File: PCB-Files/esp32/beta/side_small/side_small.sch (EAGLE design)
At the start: 9 parts

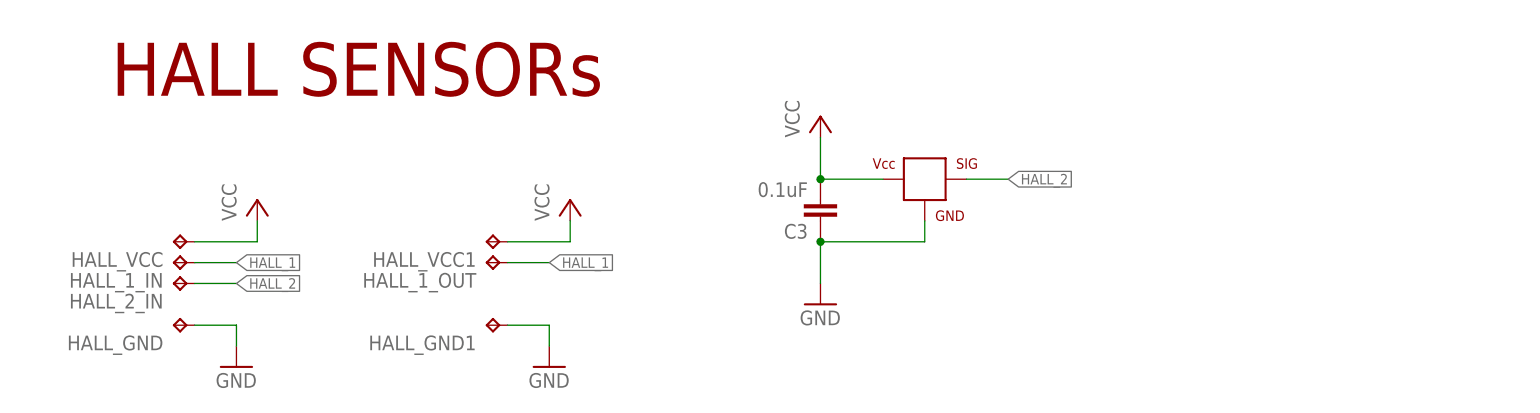
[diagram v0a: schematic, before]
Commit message: creates final PCB version; revised beta side pcbs to match beta main pcb pinouts
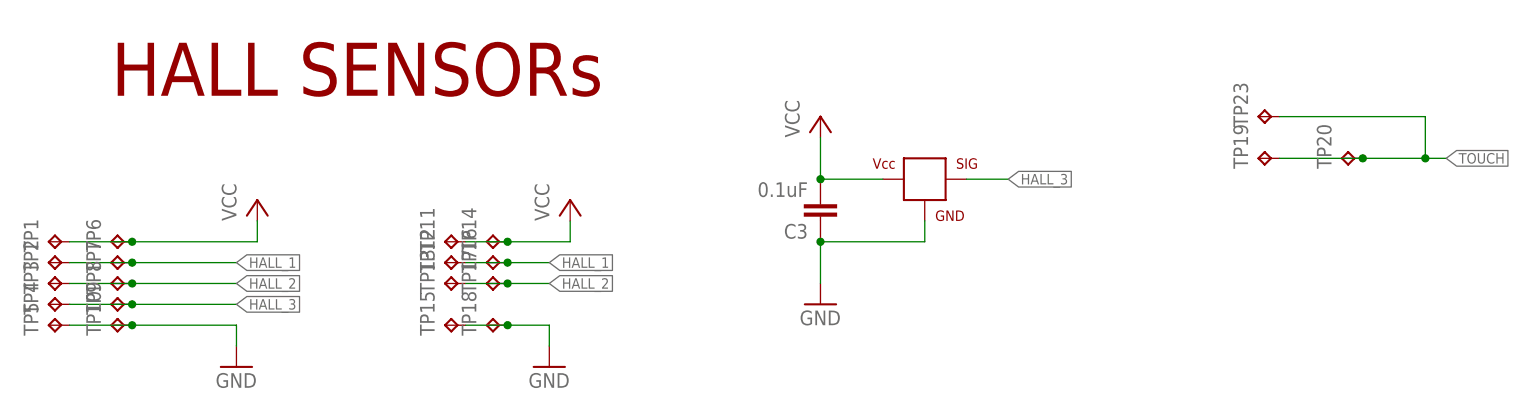
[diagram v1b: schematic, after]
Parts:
- removed HALL_1_IN, HALL_1_OUT, HALL_2_IN, HALL_GND, HALL_GND1, HALL_VCC, HALL_VCC1: TPTP20SQ, testpad:TPTP20SQ
- added TP1, TP10, TP11, TP12, TP13, TP14, TP15, TP16, TP17, TP18, TP19, TP2, TP20, TP23, TP3, TP4, TP5, TP6, TP7, TP8, TP9: TPTP10SQ, testpad:TPTP10SQ
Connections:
- new net HALL_3: HALL.SIG, TP4.TP, TP9.TP
- new net TOUCH: TP19.TP, TP20.TP, TP23.TP
- net GND: now also TP10.TP, TP15.TP, TP18.TP, TP5.TP; no longer HALL_GND.TP, HALL_GND1.TP
- net HALL_1: now also TP12.TP, TP16.TP, TP2.TP, TP7.TP; no longer HALL_1_IN.TP, HALL_1_OUT.TP
- net HALL_2: now also TP13.TP, TP17.TP, TP3.TP, TP8.TP; no longer HALL.SIG, HALL_2_IN.TP
- net VCC: now also TP1.TP, TP11.TP, TP14.TP, TP6.TP; no longer HALL_VCC.TP, HALL_VCC1.TP
